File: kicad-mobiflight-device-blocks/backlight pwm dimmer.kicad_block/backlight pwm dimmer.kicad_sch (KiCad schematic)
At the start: 3 parts, among them Q2 2N7000

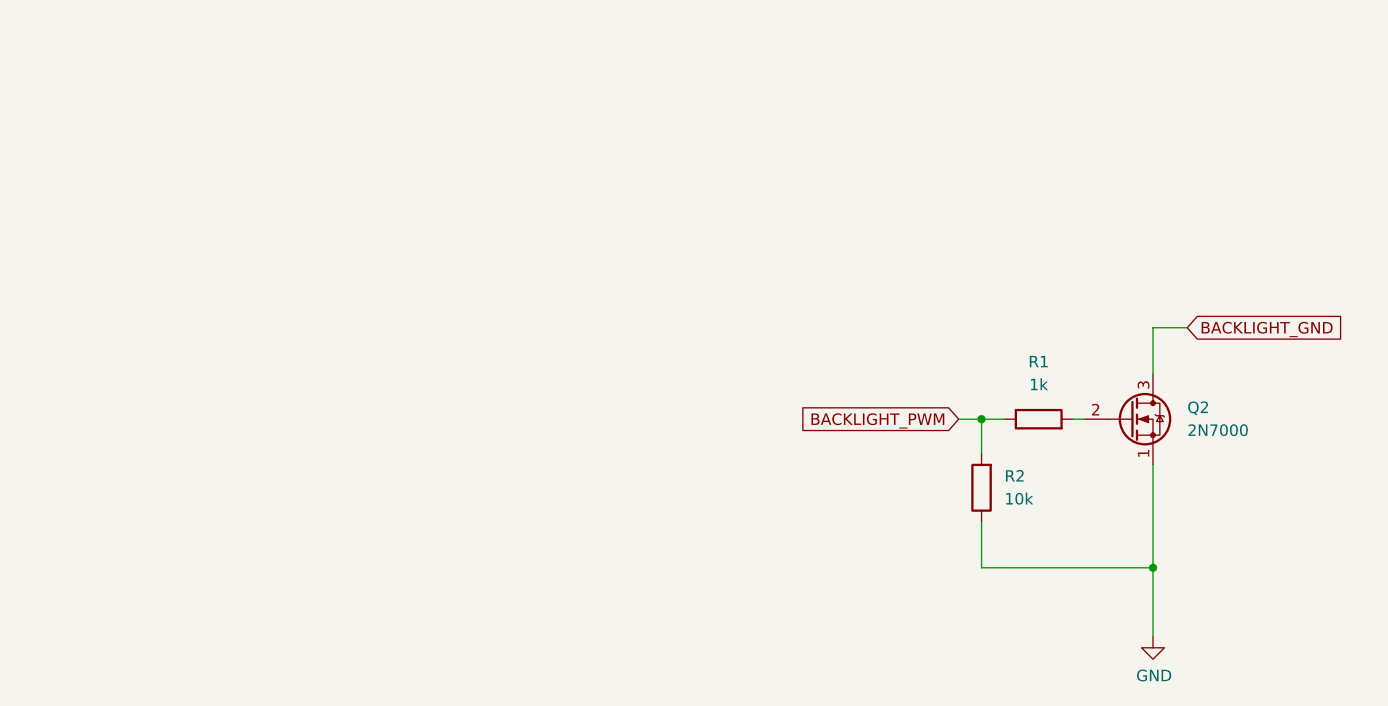
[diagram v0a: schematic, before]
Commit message: use IRLZ44N mosfet for design block
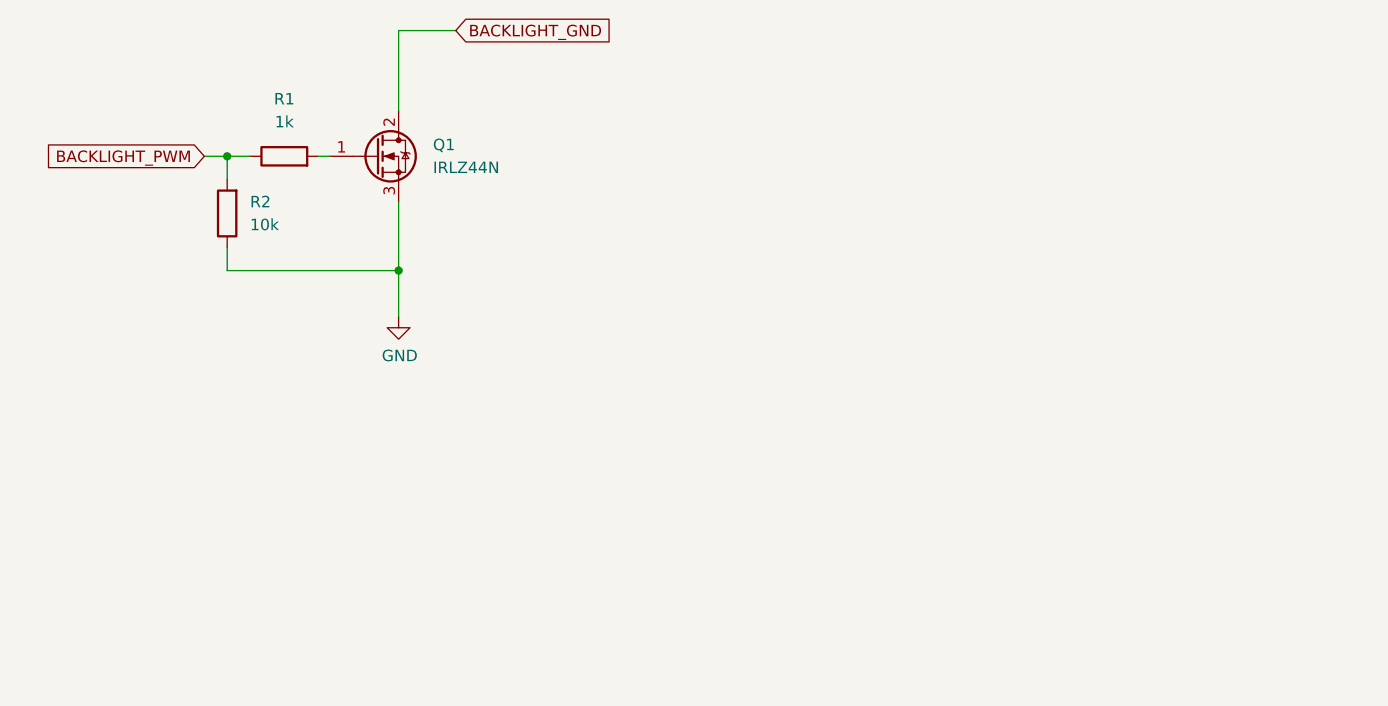
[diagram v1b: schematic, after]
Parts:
- removed Q2: 2N7000, Package_TO_SOT_THT:TO-92L_Inline_Wide, symbol Transistor_FET:2N7000
- added Q1: IRLZ44N, Package_TO_SOT_THT:TO-220-3_Horizontal_TabDown, symbol Transistor_FET:IRLZ44N
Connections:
- net BACKLIGHT_GND: now also Q1.2 (D)
- net GND: now also Q1.3 (S)
- net at R1.2: now also Q1.1 (G)
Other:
- moved on the sheet: R1, R2
